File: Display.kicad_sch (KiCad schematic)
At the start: 14 parts, among them Q1 MMBT2222ALT1G, U7 TSC2046IPWR_C8954

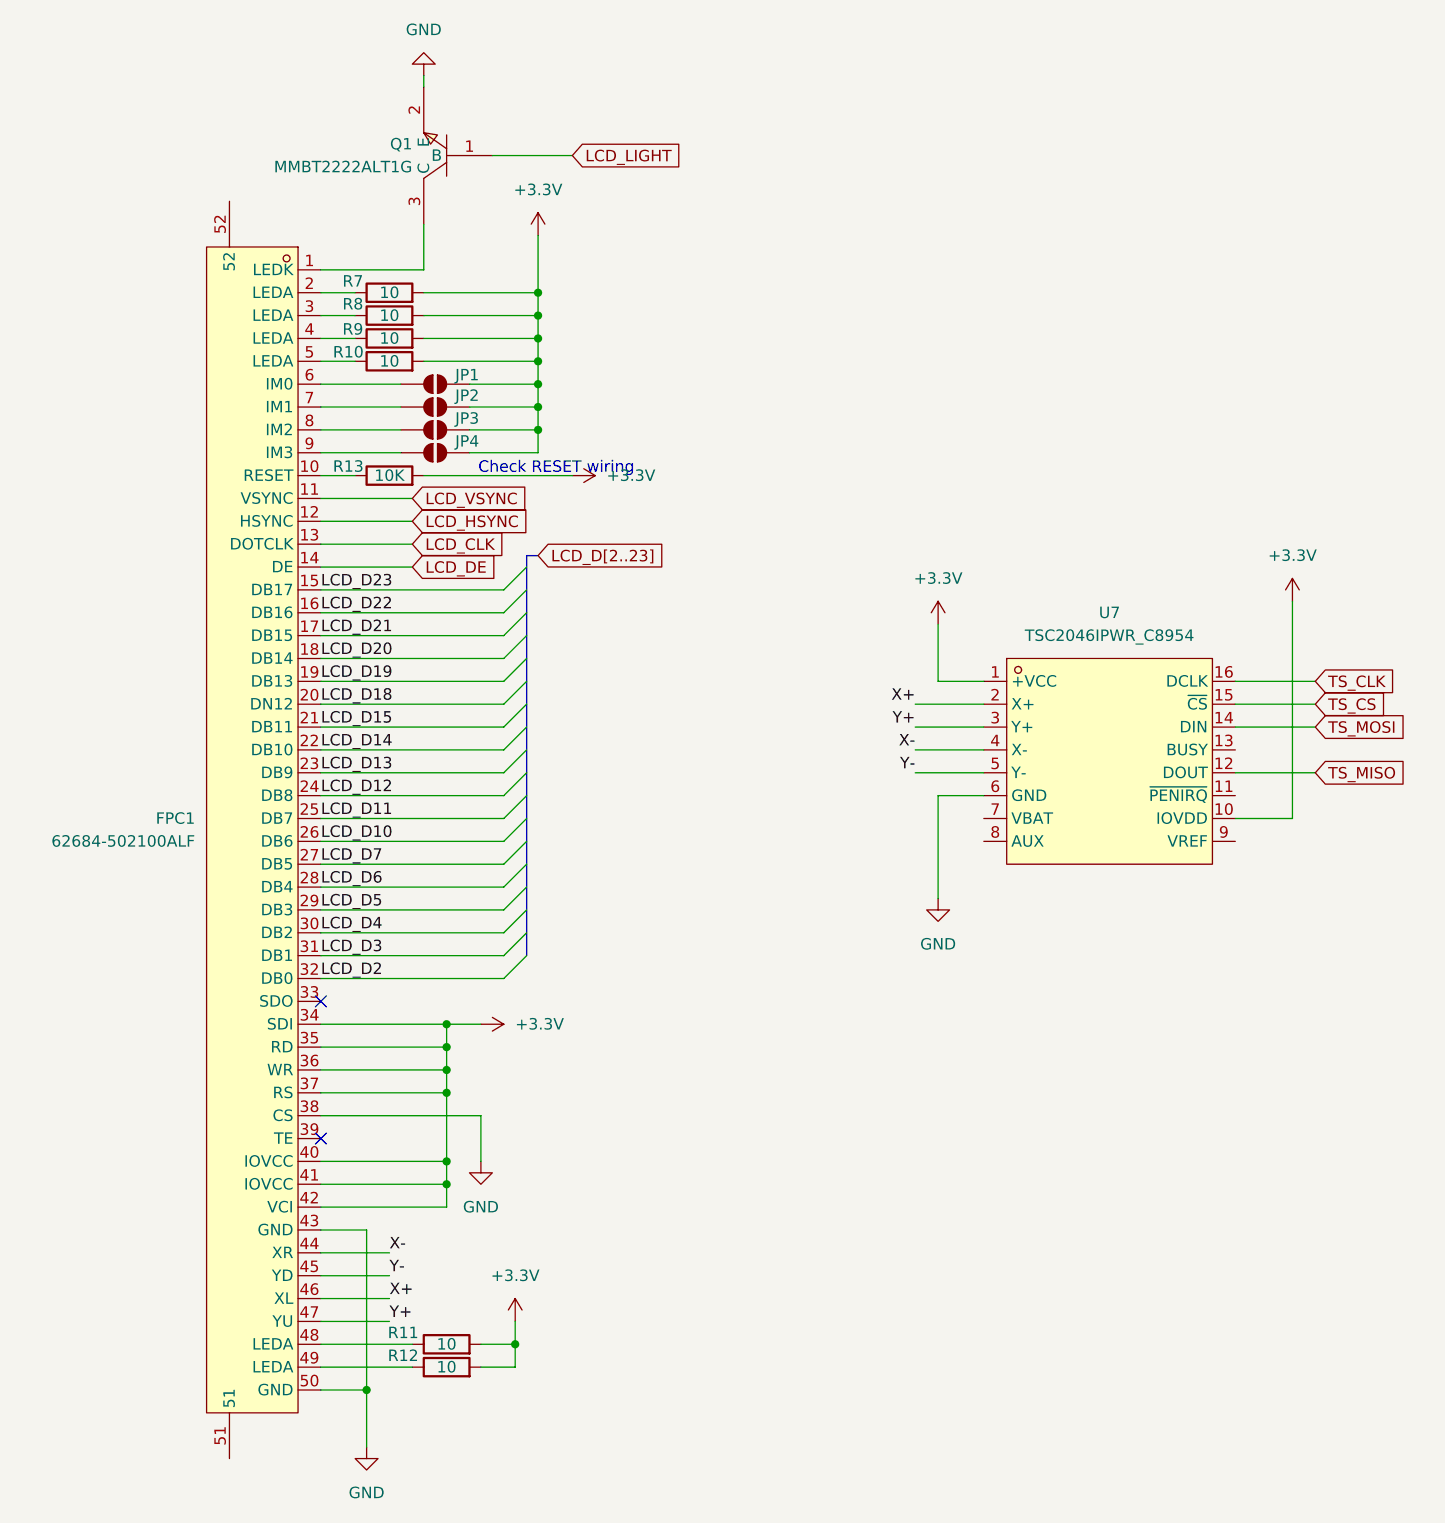
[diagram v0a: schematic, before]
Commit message: power changes, audio changes, testing layout
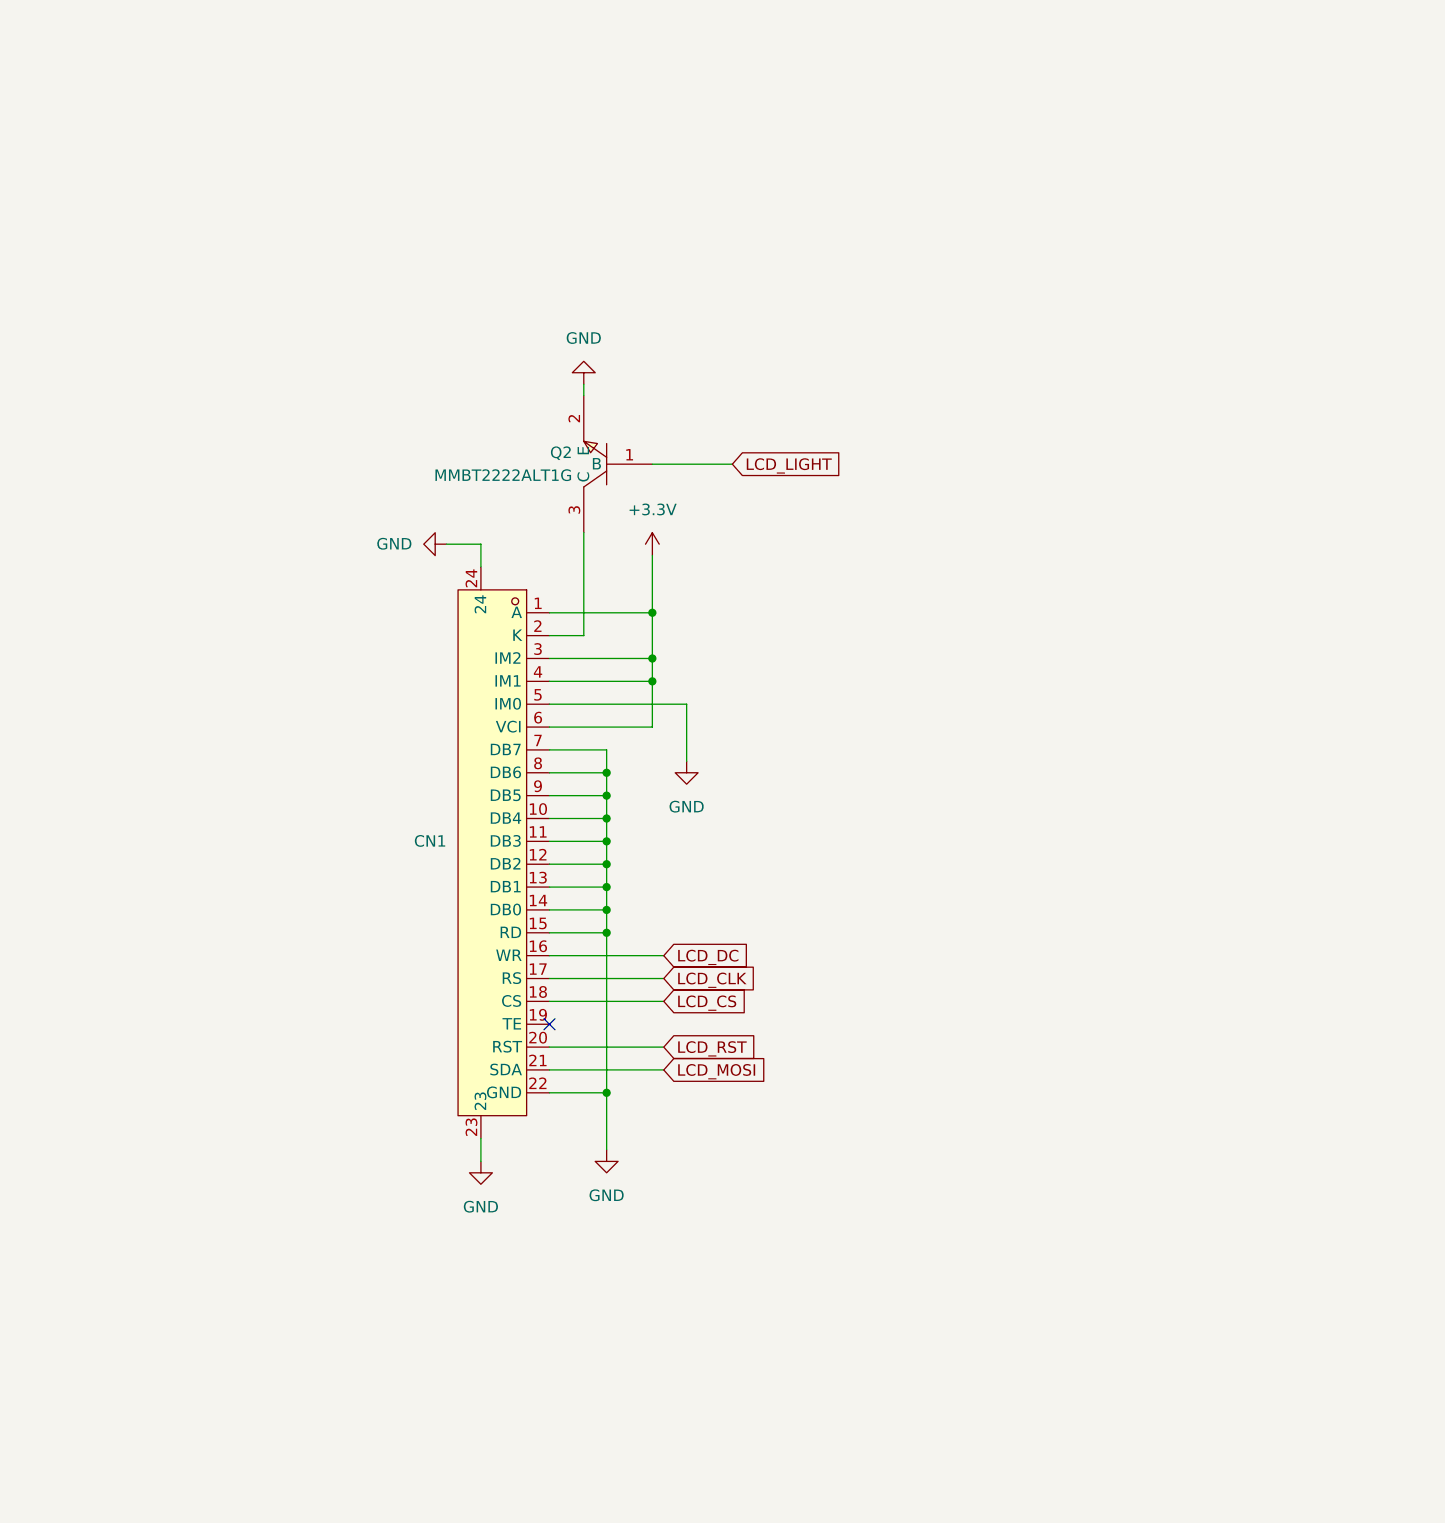
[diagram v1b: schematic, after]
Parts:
- removed FPC1: 62684-502100ALF, easyeda2kicad:FPC-SMD_50P-P0.50_62684-501100ALF, symbol easyeda2kicad:62684-502100ALF
- removed JP1, JP2, JP3, JP4: SolderJumper_2_Open, Jumper:SolderJumper-2_P1.3mm_Open_TrianglePad1.0x1.5mm, symbol Jumper:SolderJumper_2_Open
- removed Q1: MMBT2222ALT1G, easyeda2kicad:SOT-23-3_L2.9-W1.3-P1.90-LS2.4-BR, symbol easyeda2kicad:MMBT2222ALT1G
- removed R10, R11, R12, R7, R8, R9: 10, symbol Device:R
- removed R13: 10K, symbol Device:R
- removed U7: TSC2046IPWR_C8954, easyeda2kicad:TSSOP-16_L5.0-W4.4-P0.65-LS6.4-BL, symbol easyeda2kicad:TSC2046IPWR_C8954
- added CN1: HC-FPC-05-09-22RLTAG, easyeda2kicad:CONN-SMD_22P-P0.50_HCTL_HC-FPC-05-09-22RLTAG, symbol easyeda2kicad:HC-FPC-05-09-22RLTAG
- added Q2: MMBT2222ALT1G, easyeda2kicad:SOT-23-3_L2.9-W1.3-P1.90-LS2.4-BR, symbol easyeda2kicad:MMBT2222ALT1G
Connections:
- net +3.3V: now also CN1.1 (A), CN1.3 (IM2), CN1.4 (IM1), CN1.6 (VCI)
- net GND: now also CN1.10 (DB4), CN1.11 (DB3), CN1.12 (DB2), CN1.13 (DB1), CN1.14 (DB0), CN1.15 (RD), CN1.22 (GND), CN1.23, CN1.24, CN1.5 (IM0), CN1.7 (DB7), CN1.8 (DB6), CN1.9 (DB5), Q2.2 (E)
- net LCD_CLK: now also CN1.17 (RS)
- net LCD_LIGHT: now also Q2.1 (B)
- new net: CN1.2 (K), Q2.3 (C)
- new net LCD_CS: CN1.18 (CS)
- new net LCD_DC: CN1.16 (WR)
- new net LCD_MOSI: CN1.21 (SDA)
- new net LCD_RST: CN1.20 (RST)
- no-connect marks 2 -> 1
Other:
- note removed: "Check RESET wiring"

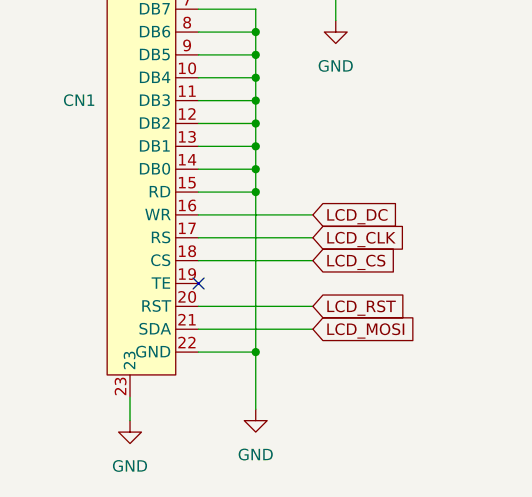
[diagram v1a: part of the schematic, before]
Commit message: audio changes, better layout
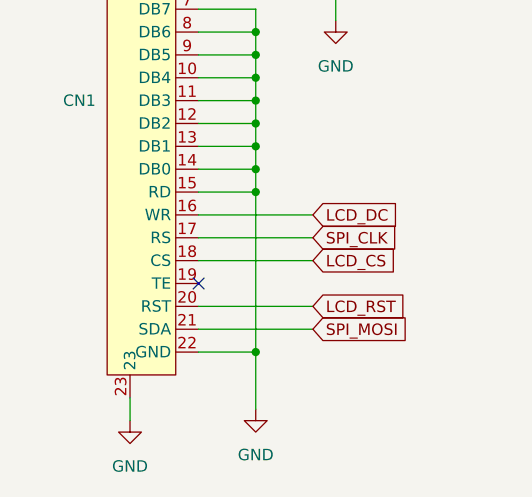
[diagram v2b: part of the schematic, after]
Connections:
- net LCD_CLK renamed SPI_CLK
- net LCD_MOSI renamed SPI_MOSI
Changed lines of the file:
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@@
 		)
 	)
-	(global_label "LCD_MOSI"
+	(global_label "SPI_MOSI"
 		(shape input)
 		(at 93.98 132.08 0)
@@
 		)
 		(property "Intersheetrefs" "${INTERSHEET_REFS}"
-			(at 106.0971 132.08 0)
+			(at 105.6133 132.08 0)
 			(effects
 				(font
@@
 		)
 	)
-	(global_label "LCD_CLK"
+	(global_label "SPI_CLK"
 		(shape input)
 		(at 93.98 121.92 0)
@@
 		)
 		(property "Intersheetrefs" "${INTERSHEET_REFS}"
-			(at 105.069 121.92 0)
+			(at 104.5852 121.92 0)
 			(effects
 				(font

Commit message: power changes for v3s, cleanup
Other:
- title: (none) -> iPodClone
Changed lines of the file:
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@@
 	(generator_version "9.0")
 	(paper "A4")
+	(title_block
+		(title "iPodClone")
+		(rev "1.0")
+		(comment 1 "22pin FPC connection to 1.54\" LCD display")
+	)
 	(junction
 		(at 92.71 81.28)
